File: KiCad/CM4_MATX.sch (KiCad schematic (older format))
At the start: 9 parts

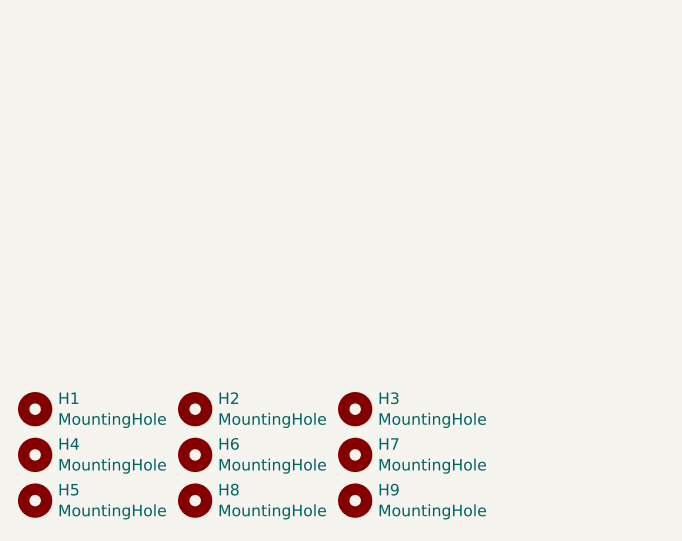
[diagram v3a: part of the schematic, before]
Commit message: Updated CM4 footprints/symbols, mounting holes
This is in a bid to make it more manufactuerable by reducing the need for explanations and questions.
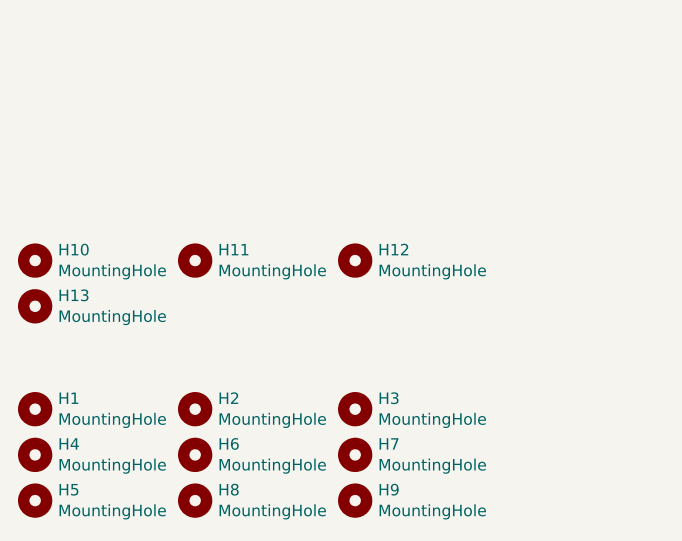
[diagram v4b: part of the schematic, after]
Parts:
- added H10, H11, H12, H13: MountingHole, MountingHole:MountingHole_2.7mm_M2.5, symbol Mechanical:MountingHole
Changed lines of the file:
@@
 Sheet 1 16
 Title "CM4 MATX Root Sheet"
-Date "2020-12-28"
+Date "2021-02-08"
 Rev "0.1"
 Comp "Copyright Oliver Møller/@TheGuyDanish 2020, CERN OHL-P v2"
@@
 Wire Wire Line
 	6950 2300 7300 2300
+$Comp
+L Mechanical:MountingHole H10
+U 1 1 60295E06
+P 650 6550
+F 0 "H10" H 750 6596 50  0000 L CNN
+F 1 "MountingHole" H 750 6505 50  0000 L CNN
+F 2 "MountingHole:MountingHole_2.7mm_M2.5" H 650 6550 50  0001 C CNN
+F 3 "~" H 650 6550 50  0001 C CNN
+	1    650  6550
+	1    0    0    -1
+$EndComp
+$Comp
+L Mechanical:MountingHole H11
+U 1 1 60295FE4
+P 1350 6550
+F 0 "H11" H 1450 6596 50  0000 L CNN
+F 1 "MountingHole" H 1450 6505 50  0000 L CNN
+F 2 "MountingHole:MountingHole_2.7mm_M2.5" H 1350 6550 50  0001 C CNN
+F 3 "~" H 1350 6550 50  0001 C CNN
+	1    1350 6550
+	1    0    0    -1
+$EndComp
+$Comp
+L Mechanical:MountingHole H12
+U 1 1 602961DC
+P 2050 6550
+F 0 "H12" H 2150 6596 50  0000 L CNN
+F 1 "MountingHole" H 2150 6505 50  0000 L CNN
+F 2 "MountingHole:MountingHole_2.7mm_M2.5" H 2050 6550 50  0001 C CNN
+F 3 "~" H 2050 6550 50  0001 C CNN
+	1    2050 6550
+	1    0    0    -1
+$EndComp
+$Comp
+L Mechanical:MountingHole H13
+U 1 1 60296317
+P 650 6750
+F 0 "H13" H 750 6796 50  0000 L CNN
+F 1 "MountingHole" H 750 6705 50  0000 L CNN
+F 2 "MountingHole:MountingHole_2.7mm_M2.5" H 650 6750 50  0001 C CNN
+F 3 "~" H 650 6750 50  0001 C CNN
+	1    650  6750
+	1    0    0    -1
+$EndComp
 $EndSCHEMATC

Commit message: Started picking passive components, overhauled library
Cleaned up a bunch of schematic library references.
Added datasheets, descriptions for a lot of existing parts.
Picked most capacitor parts, still a couple left.
Cleaned up a fair few footprint references.
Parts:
- H1, H2, H3, H4, H5, H6, H7, H8, H9: footprint MountingHole:MountingHole_3.2mm_M3_Pad_Via -> CM4_MATX:MountingHole_3.2mm_M3_Pad_Via; symbol Mechanical:MountingHole -> CM4_MATX:MountingHole; Description (none) -> mATX Mounting Holes
- H10, H11, H12, H13: footprint MountingHole:MountingHole_2.7mm_M2.5 -> CM4_MATX:MountingHole_2.7mm_M2.5; symbol Mechanical:MountingHole -> CM4_MATX:MountingHole; Description (none) -> Pi CM4 Mounting Holes
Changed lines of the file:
@@
 $EndSheet
 $Comp
-L Mechanical:MountingHole H1
+L CM4_MATX:MountingHole H1
 U 1 1 5FB6444A
 P 650 7200
 F 0 "H1" H 750 7246 50  0000 L CNN
 F 1 "MountingHole" H 750 7155 50  0000 L CNN
-F 2 "MountingHole:MountingHole_3.2mm_M3_Pad_Via" H 650 7200 50  0001 C CNN
-F 3 "~" H 650 7200 50  0001 C CNN
+F 2 "CM4_MATX:MountingHole_3.2mm_M3_Pad_Via" H 650 7200 50  0001 C CNN
+F 3 "https://doc.xdevs.com/doc/_PC_HW/Form_factors/matxspe1.2.pdf" H 650 7200 50  0001 C CNN
+F 4 "mATX Mounting Holes" H 650 7200 50  0001 C CNN "Description"
 	1    650  7200
 	1    0    0    -1
 $EndComp
 $Comp
-L Mechanical:MountingHole H2
+L CM4_MATX:MountingHole H2
 U 1 1 5FB649F9
 P 1350 7200
 F 0 "H2" H 1450 7246 50  0000 L CNN
 F 1 "MountingHole" H 1450 7155 50  0000 L CNN
-F 2 "MountingHole:MountingHole_3.2mm_M3_Pad_Via" H 1350 7200 50  0001 C CNN
-F 3 "~" H 1350 7200 50  0001 C CNN
+F 2 "CM4_MATX:MountingHole_3.2mm_M3_Pad_Via" H 1350 7200 50  0001 C CNN
+F 3 "https://doc.xdevs.com/doc/_PC_HW/Form_factors/matxspe1.2.pdf" H 1350 7200 50  0001 C CNN
+F 4 "mATX Mounting Holes" H 1350 7200 50  0001 C CNN "Description"
 	1    1350 7200
 	1    0    0    -1
 $EndComp
 $Comp
-L Mechanical:MountingHole H3
+L CM4_MATX:MountingHole H3
 U 1 1 5FB64C61
 P 2050 7200
 F 0 "H3" H 2150 7246 50  0000 L CNN
 F 1 "MountingHole" H 2150 7155 50  0000 L CNN
-F 2 "MountingHole:MountingHole_3.2mm_M3_Pad_Via" H 2050 7200 50  0001 C CNN
-F 3 "~" H 2050 7200 50  0001 C CNN
+F 2 "CM4_MATX:MountingHole_3.2mm_M3_Pad_Via" H 2050 7200 50  0001 C CNN
+F 3 "https://doc.xdevs.com/doc/_PC_HW/Form_factors/matxspe1.2.pdf" H 2050 7200 50  0001 C CNN
+F 4 "mATX Mounting Holes" H 2050 7200 50  0001 C CNN "Description"
 	1    2050 7200
 	1    0    0    -1
 $EndComp
 $Comp
-L Mechanical:MountingHole H4
+L CM4_MATX:MountingHole H4
 U 1 1 5FB658C2
 P 650 7400
 F 0 "H4" H 750 7446 50  0000 L CNN
 F 1 "MountingHole" H 750 7355 50  0000 L CNN
-F 2 "MountingHole:MountingHole_3.2mm_M3_Pad_Via" H 650 7400 50  0001 C CNN
-F 3 "~" H 650 7400 50  0001 C CNN
+F 2 "CM4_MATX:MountingHole_3.2mm_M3_Pad_Via" H 650 7400 50  0001 C CNN
+F 3 "https://doc.xdevs.com/doc/_PC_HW/Form_factors/matxspe1.2.pdf" H 650 7400 50  0001 C CNN
+F 4 "mATX Mounting Holes" H 650 7400 50  0001 C CNN "Description"
 	1    650  7400
 	1    0    0    -1
 $EndComp
 $Comp
-L Mechanical:MountingHole H5
+L CM4_MATX:MountingHole H5
 U 1 1 5FB65A47
 P 650 7600
 F 0 "H5" H 750 7646 50  0000 L CNN
 F 1 "MountingHole" H 750 7555 50  0000 L CNN
-F 2 "MountingHole:MountingHole_3.2mm_M3_Pad_Via" H 650 7600 50  0001 C CNN
-F 3 "~" H 650 7600 50  0001 C CNN
+F 2 "CM4_MATX:MountingHole_3.2mm_M3_Pad_Via" H 650 7600 50  0001 C CNN
+F 3 "https://doc.xdevs.com/doc/_PC_HW/Form_factors/matxspe1.2.pdf" H 650 7600 50  0001 C CNN
+F 4 "mATX Mounting Holes" H 650 7600 50  0001 C CNN "Description"
 	1    650  7600
 	1    0    0    -1
 $EndComp
 $Comp
-L Mechanical:MountingHole H6
+L CM4_MATX:MountingHole H6
 U 1 1 5FB65B17
 P 1350 7400
 F 0 "H6" H 1450 7446 50  0000 L CNN
 F 1 "MountingHole" H 1450 7355 50  0000 L CNN
-F 2 "MountingHole:MountingHole_3.2mm_M3_Pad_Via" H 1350 7400 50  0001 C CNN
-F 3 "~" H 1350 7400 50  0001 C CNN
+F 2 "CM4_MATX:MountingHole_3.2mm_M3_Pad_Via" H 1350 7400 50  0001 C CNN
+F 3 "https://doc.xdevs.com/doc/_PC_HW/Form_factors/matxspe1.2.pdf" H 1350 7400 50  0001 C CNN
+F 4 "mATX Mounting Holes" H 1350 7400 50  0001 C CNN "Description"
 	1    1350 7400
 	1    0    0    -1
 $EndComp
 $Comp
-L Mechanical:MountingHole H7
+L CM4_MATX:MountingHole H7
 U 1 1 5FB65D40
 P 2050 7400
 F 0 "H7" H 2150 7446 50  0000 L CNN
 F 1 "MountingHole" H 2150 7355 50  0000 L CNN
-F 2 "MountingHole:MountingHole_3.2mm_M3_Pad_Via" H 2050 7400 50  0001 C CNN
-F 3 "~" H 2050 7400 50  0001 C CNN
+F 2 "CM4_MATX:MountingHole_3.2mm_M3_Pad_Via" H 2050 7400 50  0001 C CNN
+F 3 "https://doc.xdevs.com/doc/_PC_HW/Form_factors/matxspe1.2.pdf" H 2050 7400 50  0001 C CNN
+F 4 "mATX Mounting Holes" H 2050 7400 50  0001 C CNN "Description"
 	1    2050 7400
 	1    0    0    -1
 $EndComp
 $Comp
-L Mechanical:MountingHole H9
+L CM4_MATX:MountingHole H9
 U 1 1 5FB65FD3
 P 2050 7600
 F 0 "H9" H 2150 7646 50  0000 L CNN
 F 1 "MountingHole" H 2150 7555 50  0000 L CNN
-F 2 "MountingHole:MountingHole_3.2mm_M3_Pad_Via" H 2050 7600 50  0001 C CNN
-F 3 "~" H 2050 7600 50  0001 C CNN
+F 2 "CM4_MATX:MountingHole_3.2mm_M3_Pad_Via" H 2050 7600 50  0001 C CNN
+F 3 "https://doc.xdevs.com/doc/_PC_HW/Form_factors/matxspe1.2.pdf" H 2050 7600 50  0001 C CNN
+F 4 "mATX Mounting Holes" H 2050 7600 50  0001 C CNN "Description"
 	1    2050 7600
 	1    0    0    -1
 $EndComp
 $Comp
-L Mechanical:MountingHole H8
+L CM4_MATX:MountingHole H8
 U 1 1 5FB66182
 P 1350 7600
 F 0 "H8" H 1450 7646 50  0000 L CNN
 F 1 "MountingHole" H 1450 7555 50  0000 L CNN
-F 2 "MountingHole:MountingHole_3.2mm_M3_Pad_Via" H 1350 7600 50  0001 C CNN
-F 3 "~" H 1350 7600 50  0001 C CNN
+F 2 "CM4_MATX:MountingHole_3.2mm_M3_Pad_Via" H 1350 7600 50  0001 C CNN
+F 3 "https://doc.xdevs.com/doc/_PC_HW/Form_factors/matxspe1.2.pdf" H 1350 7600 50  0001 C CNN
+F 4 "mATX Mounting Holes" H 1350 7600 50  0001 C CNN "Description"
 	1    1350 7600
 	1    0    0    -1
@@
 	6950 2300 7300 2300
 $Comp
-L Mechanical:MountingHole H10
+L CM4_MATX:MountingHole H10
 U 1 1 60295E06
 P 650 6550
 F 0 "H10" H 750 6596 50  0000 L CNN
 F 1 "MountingHole" H 750 6505 50  0000 L CNN
-F 2 "MountingHole:MountingHole_2.7mm_M2.5" H 650 6550 50  0001 C CNN
-F 3 "~" H 650 6550 50  0001 C CNN
+F 2 "CM4_MATX:MountingHole_2.7mm_M2.5" H 650 6550 50  0001 C CNN
+F 3 "https://datasheets.raspberrypi.org/cm4/cm4-datasheet.pdf" H 650 6550 50  0001 C CNN
+F 4 "Pi CM4 Mounting Holes" H 650 6550 50  0001 C CNN "Description"
 	1    650  6550
 	1    0    0    -1
 $EndComp
 $Comp
-L Mechanical:MountingHole H11
+L CM4_MATX:MountingHole H11
 U 1 1 60295FE4
 P 1350 6550
 F 0 "H11" H 1450 6596 50  0000 L CNN
 F 1 "MountingHole" H 1450 6505 50  0000 L CNN
-F 2 "MountingHole:MountingHole_2.7mm_M2.5" H 1350 6550 50  0001 C CNN
-F 3 "~" H 1350 6550 50  0001 C CNN
+F 2 "CM4_MATX:MountingHole_2.7mm_M2.5" H 1350 6550 50  0001 C CNN
+F 3 "https://datasheets.raspberrypi.org/cm4/cm4-datasheet.pdf" H 1350 6550 50  0001 C CNN
+F 4 "Pi CM4 Mounting Holes" H 1350 6550 50  0001 C CNN "Description"
 	1    1350 6550
 	1    0    0    -1
 $EndComp
 $Comp
-L Mechanical:MountingHole H12
+L CM4_MATX:MountingHole H12
 U 1 1 602961DC
 P 2050 6550
 F 0 "H12" H 2150 6596 50  0000 L CNN
 F 1 "MountingHole" H 2150 6505 50  0000 L CNN
-F 2 "MountingHole:MountingHole_2.7mm_M2.5" H 2050 6550 50  0001 C CNN
-F 3 "~" H 2050 6550 50  0001 C CNN
+F 2 "CM4_MATX:MountingHole_2.7mm_M2.5" H 2050 6550 50  0001 C CNN
+F 3 "https://datasheets.raspberrypi.org/cm4/cm4-datasheet.pdf" H 2050 6550 50  0001 C CNN
+F 4 "Pi CM4 Mounting Holes" H 2050 6550 50  0001 C CNN "Description"
 	1    2050 6550
 	1    0    0    -1
 $EndComp
 $Comp
-L Mechanical:MountingHole H13
+L CM4_MATX:MountingHole H13
 U 1 1 60296317
 P 650 6750
 F 0 "H13" H 750 6796 50  0000 L CNN
 F 1 "MountingHole" H 750 6705 50  0000 L CNN
-F 2 "MountingHole:MountingHole_2.7mm_M2.5" H 650 6750 50  0001 C CNN
-F 3 "~" H 650 6750 50  0001 C CNN
+F 2 "CM4_MATX:MountingHole_2.7mm_M2.5" H 650 6750 50  0001 C CNN
+F 3 "https://datasheets.raspberrypi.org/cm4/cm4-datasheet.pdf" H 650 6750 50  0001 C CNN
+F 4 "Pi CM4 Mounting Holes" H 650 6750 50  0001 C CNN "Description"
 	1    650  6750
 	1    0    0    -1
